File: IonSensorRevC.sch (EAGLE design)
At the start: 19 parts, among them U1 REF2033AIDDCT, U2 INA826AIDR, U3 INA826AIDR, U4 INA826AIDR, X1 SFV4R-1STE1LF

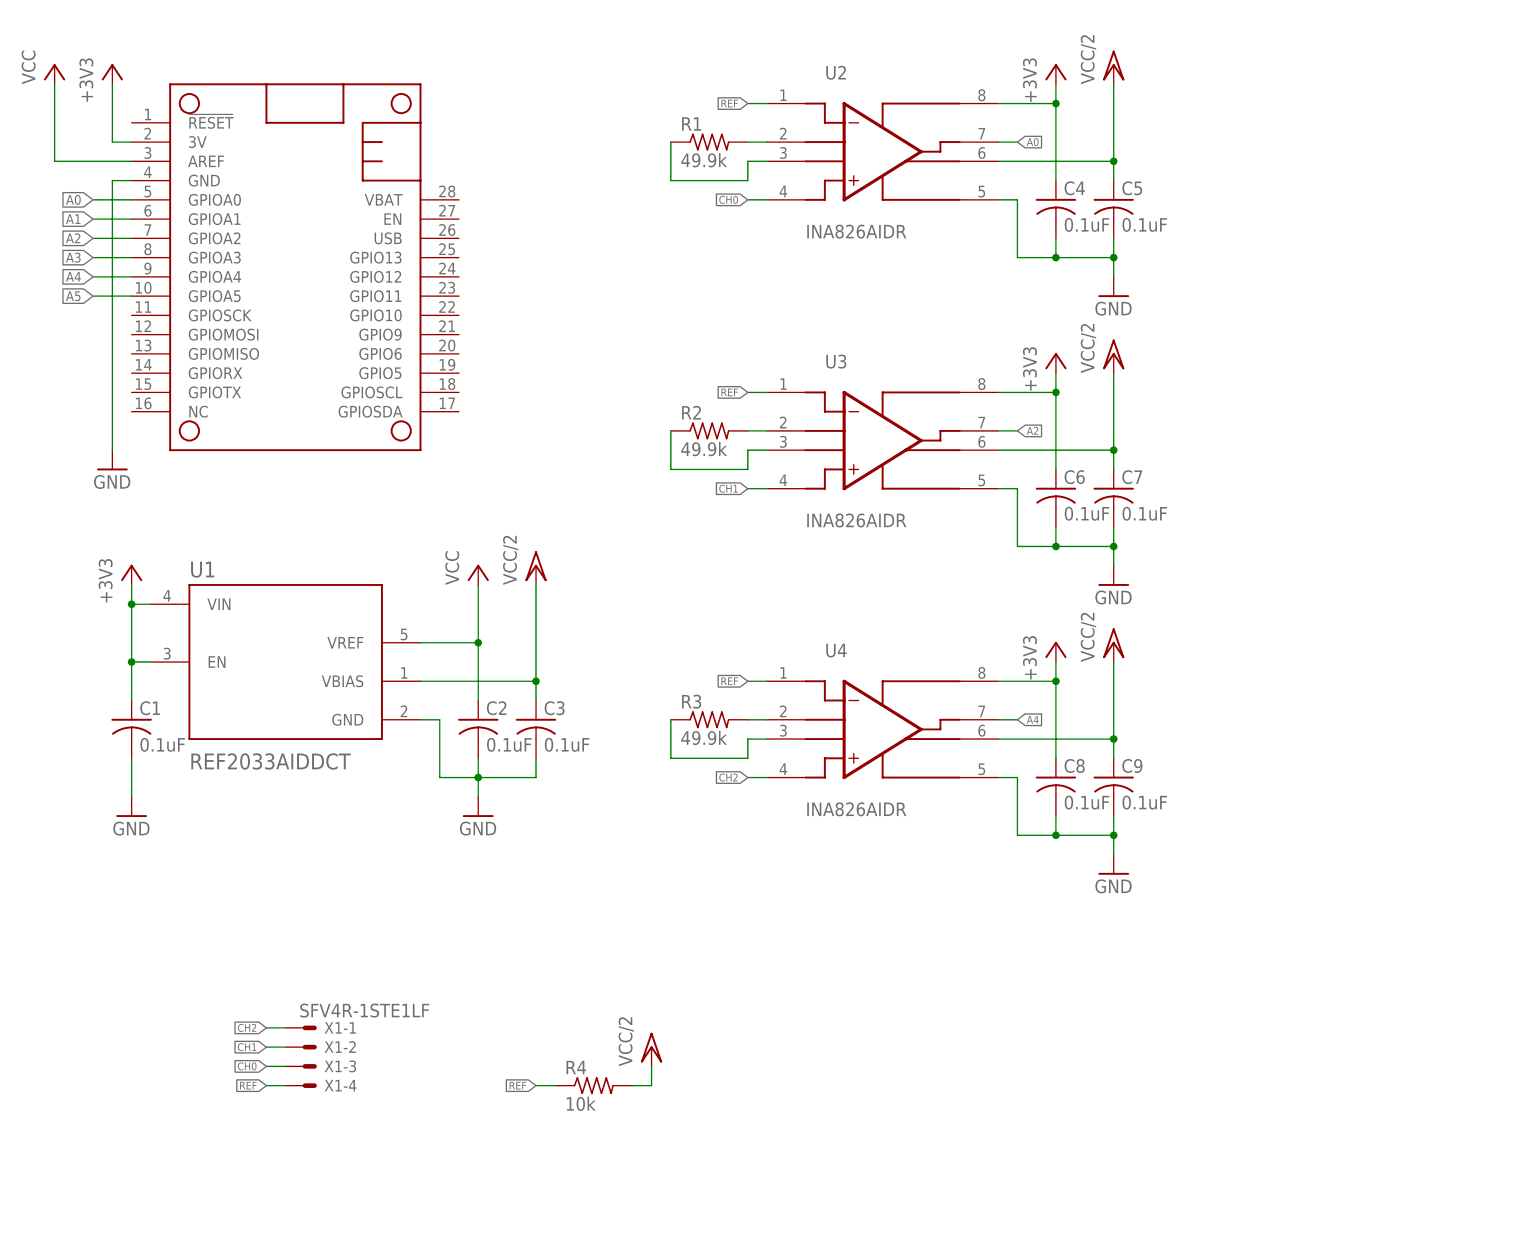
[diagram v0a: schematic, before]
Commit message: Update traces
Updated traces to minimize noise
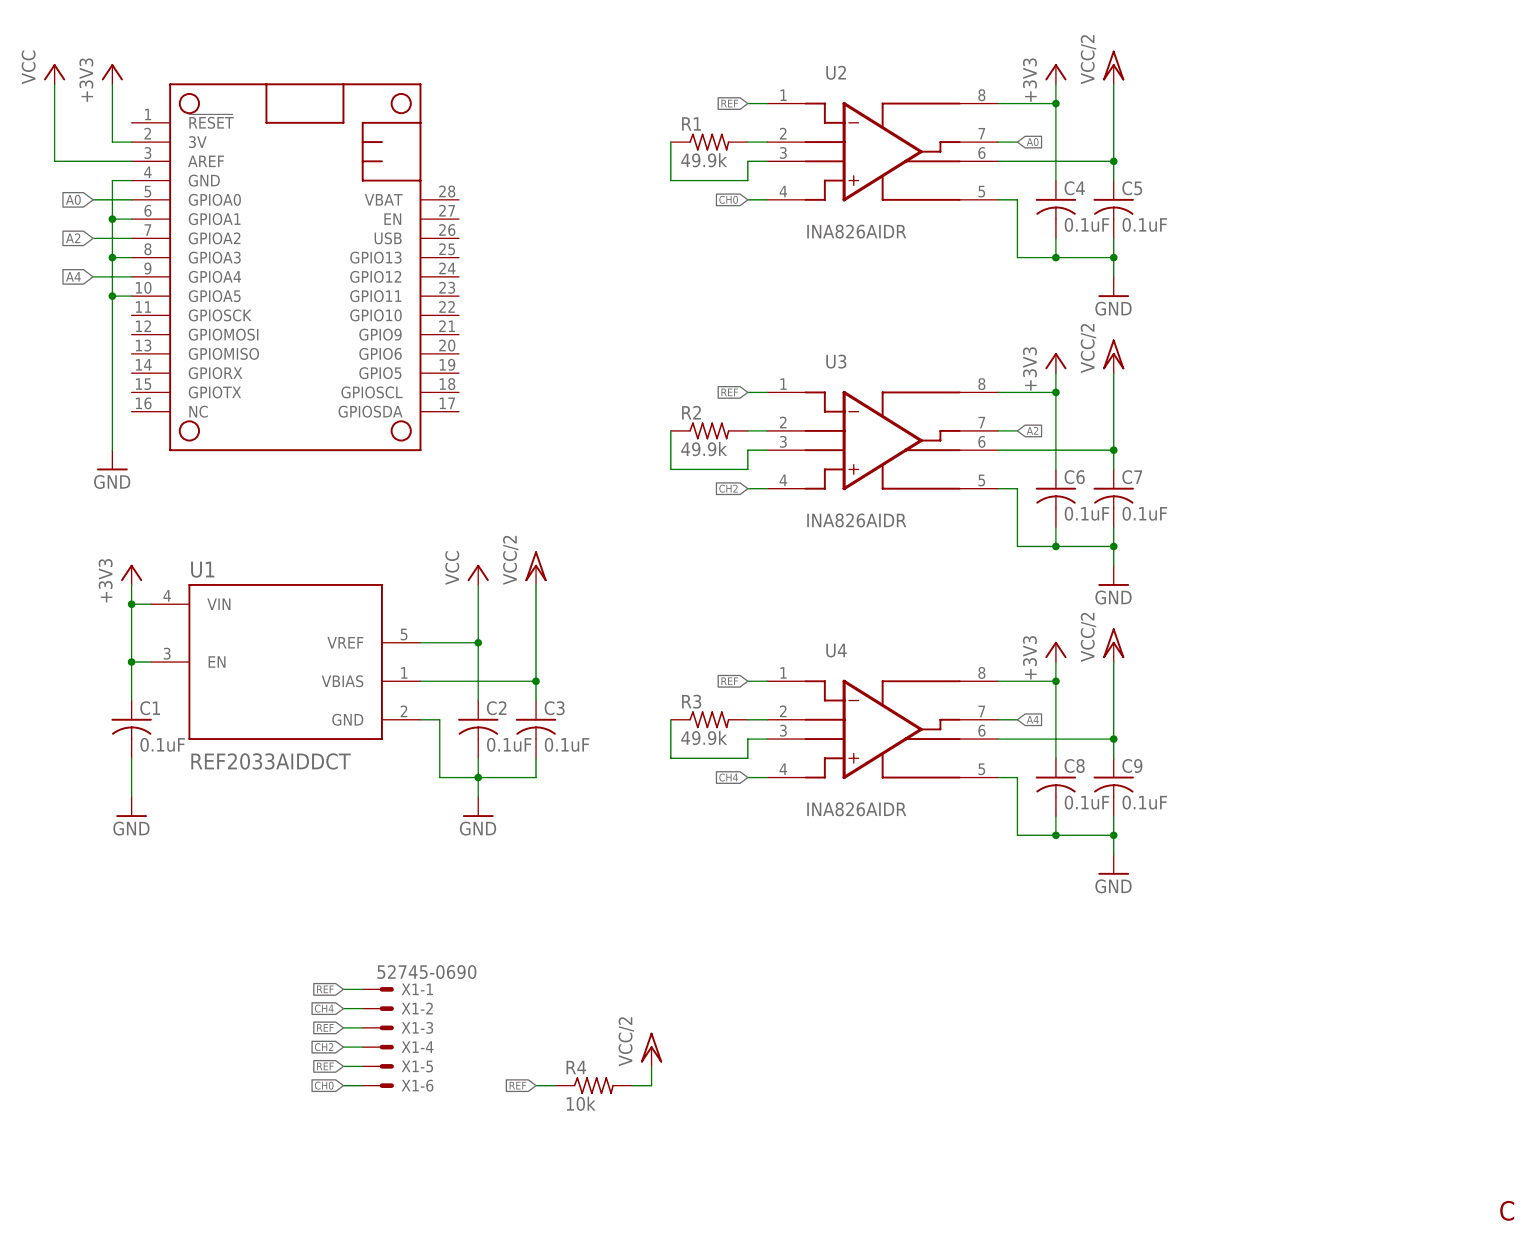
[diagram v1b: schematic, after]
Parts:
- X1: value SFV4R-1STE1LF -> 52745-0690; device adafruit:SFV4R-1STE1LF -> con-molex:52745-0690
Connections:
- removed net A1: MS1.GPIOA1
- removed net A3: MS1.GPIOA3
- removed net A5: MS1.GPIOA5
- removed net CH1: U3.+IN, X1-2.S
- new net CH4: U4.+IN, X1-2.S
- net CH0: now also X1-6.S; no longer X1-3.S
- net CH2: now also U3.+IN, X1-4.S; no longer U4.+IN, X1-1.S
- net GND: now also MS1.GPIOA1, MS1.GPIOA3, MS1.GPIOA5
- net REF: now also X1-1.S, X1-3.S, X1-5.S; no longer X1-4.S
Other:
- note added: "C"
- moved on the sheet: X1-1, X1-2, X1-3, X1-4
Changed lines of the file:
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@@
 <part name="C8" library="adafruit" library_urn="urn:adsk.eagle:library:420" deviceset="C-US" device="C0402" package3d_urn="urn:adsk.eagle:package:6240340/1" value="0.1uF"/>
 <part name="C9" library="adafruit" library_urn="urn:adsk.eagle:library:420" deviceset="C-US" device="C0402" package3d_urn="urn:adsk.eagle:package:6240340/1" value="0.1uF"/>
-<part name="X1" library="adafruit" library_urn="urn:adsk.eagle:library:420" deviceset="SFV4R-1STE1LF" device="" package3d_urn="urn:adsk.eagle:package:6240802/1"/>
 <part name="R4" library="adafruit" library_urn="urn:adsk.eagle:library:420" deviceset="R-US_" device="R0402" package3d_urn="urn:adsk.eagle:package:6240564/1" value="10k"/>
 <part name="P+7" library="supply1" library_urn="urn:adsk.eagle:library:371" deviceset="VCC/2" device=""/>
+<part name="X1" library="con-molex" library_urn="urn:adsk.eagle:library:165" deviceset="52745-0690" device="" package3d_urn="urn:adsk.eagle:package:8078608/1"/>
 </parts>
 <sheets>
 <sheet>
 <plain>
+<text x="238.76" y="7.62" size="2.54" layer="94">C</text>
 </plain>
 <instances>
@@
 <attribute name="VALUE" x="188.976" y="61.849" size="1.778" layer="96"/>
 </instance>
-<instance part="X1" gate="-1" x="81.28" y="33.02" smashed="yes">
-<attribute name="NAME" x="83.82" y="32.258" size="1.524" layer="95"/>
-<attribute name="VALUE" x="80.518" y="34.417" size="1.778" layer="96"/>
-</instance>
-<instance part="X1" gate="-2" x="81.28" y="30.48" smashed="yes">
-<attribute name="NAME" x="83.82" y="29.718" size="1.524" layer="95"/>
-</instance>
-<instance part="X1" gate="-3" x="81.28" y="27.94" smashed="yes">
-<attribute name="NAME" x="83.82" y="27.178" size="1.524" layer="95"/>
-</instance>
-<instance part="X1" gate="-4" x="81.28" y="25.4" smashed="yes">
-<attribute name="NAME" x="83.82" y="24.638" size="1.524" layer="95"/>
-</instance>
 <instance part="R4" gate="G$1" x="119.38" y="25.4" smashed="yes">
 <attribute name="NAME" x="115.57" y="26.8986" size="1.778" layer="95"/>
@@
 <instance part="P+7" gate="G$1" x="127" y="30.48" smashed="yes">
 <attribute name="VALUE" x="124.46" y="27.94" size="1.778" layer="96" rot="R90"/>
+</instance>
+<instance part="X1" gate="-1" x="91.44" y="38.1" smashed="yes">
+<attribute name="NAME" x="93.98" y="37.338" size="1.524" layer="95"/>
+<attribute name="VALUE" x="90.678" y="39.497" size="1.778" layer="96"/>
+</instance>
+<instance part="X1" gate="-2" x="91.44" y="35.56" smashed="yes">
+<attribute name="NAME" x="93.98" y="34.798" size="1.524" layer="95"/>
+</instance>
+<instance part="X1" gate="-3" x="91.44" y="33.02" smashed="yes">
+<attribute name="NAME" x="93.98" y="32.258" size="1.524" layer="95"/>
+</instance>
+<instance part="X1" gate="-4" x="91.44" y="30.48" smashed="yes">
+<attribute name="NAME" x="93.98" y="29.718" size="1.524" layer="95"/>
+</instance>
+<instance part="X1" gate="-5" x="91.44" y="27.94" smashed="yes">
+<attribute name="NAME" x="93.98" y="27.178" size="1.524" layer="95"/>
+</instance>
+<instance part="X1" gate="-6" x="91.44" y="25.4" smashed="yes">
+<attribute name="NAME" x="93.98" y="24.638" size="1.524" layer="95"/>
 </instance>
 </instances>
@@
 <wire x1="58.42" y1="144.78" x2="55.88" y2="144.78" width="0.1524" layer="91"/>
 <pinref part="GND1" gate="1" pin="GND"/>
-<wire x1="55.88" y1="144.78" x2="55.88" y2="109.22" width="0.1524" layer="91"/>
+<wire x1="55.88" y1="144.78" x2="55.88" y2="139.7" width="0.1524" layer="91"/>
+<pinref part="MS1" gate="G$1" pin="GPIOA1"/>
+<wire x1="55.88" y1="139.7" x2="55.88" y2="134.62" width="0.1524" layer="91"/>
+<wire x1="55.88" y1="134.62" x2="55.88" y2="129.54" width="0.1524" layer="91"/>
+<wire x1="55.88" y1="129.54" x2="55.88" y2="109.22" width="0.1524" layer="91"/>
+<wire x1="58.42" y1="139.7" x2="55.88" y2="139.7" width="0.1524" layer="91"/>
+<junction x="55.88" y="139.7"/>
+<pinref part="MS1" gate="G$1" pin="GPIOA3"/>
+<wire x1="58.42" y1="134.62" x2="55.88" y2="134.62" width="0.1524" layer="91"/>
+<junction x="55.88" y="134.62"/>
+<pinref part="MS1" gate="G$1" pin="GPIOA5"/>
+<wire x1="58.42" y1="129.54" x2="55.88" y2="129.54" width="0.1524" layer="91"/>
+<junction x="55.88" y="129.54"/>
 </segment>
 <segment>
@@
 </segment>
 </net>
-<net name="A1" class="0">
-<segment>
-<pinref part="MS1" gate="G$1" pin="GPIOA1"/>
-<wire x1="53.34" y1="139.7" x2="58.42" y2="139.7" width="0.1524" layer="91"/>
-<label x="53.34" y="139.7" size="1.27" layer="95" rot="R180" xref="yes"/>
-</segment>
-</net>
 <net name="A2" class="0">
 <segment>
@@
 </segment>
 </net>
-<net name="A3" class="0">
-<segment>
-<pinref part="MS1" gate="G$1" pin="GPIOA3"/>
-<wire x1="53.34" y1="134.62" x2="58.42" y2="134.62" width="0.1524" layer="91"/>
-<label x="53.34" y="134.62" size="1.27" layer="95" rot="R180" xref="yes"/>
-</segment>
-</net>
 <net name="A4" class="0">
 <segment>
@@
 <wire x1="175.26" y1="73.66" x2="172.72" y2="73.66" width="0.1524" layer="91"/>
 <label x="175.26" y="73.66" size="1.016" layer="95" xref="yes"/>
-</segment>
-</net>
-<net name="A5" class="0">
-<segment>
-<pinref part="MS1" gate="G$1" pin="GPIOA5"/>
-<wire x1="53.34" y1="129.54" x2="58.42" y2="129.54" width="0.1524" layer="91"/>
-<label x="53.34" y="129.54" size="1.27" layer="95" rot="R180" xref="yes"/>
 </segment>
 </net>
@@
 </segment>
 <segment>
-<pinref part="X1" gate="-4" pin="S"/>
-<wire x1="76.2" y1="25.4" x2="78.74" y2="25.4" width="0.1524" layer="91"/>
-<label x="76.2" y="25.4" size="1.016" layer="95" rot="R180" xref="yes"/>
-</segment>
-<segment>
 <pinref part="R4" gate="G$1" pin="1"/>
 <wire x1="111.76" y1="25.4" x2="114.3" y2="25.4" width="0.1524" layer="91"/>
 <label x="111.76" y="25.4" size="1.016" layer="95" rot="R180" xref="yes"/>
+</segment>
+<segment>
+<pinref part="X1" gate="-5" pin="S"/>
+<wire x1="86.36" y1="27.94" x2="88.9" y2="27.94" width="0.1524" layer="91"/>
+<label x="86.36" y="27.94" size="1.016" layer="95" rot="R180" xref="yes"/>
+</segment>
+<segment>
+<pinref part="X1" gate="-3" pin="S"/>
+<wire x1="86.36" y1="33.02" x2="88.9" y2="33.02" width="0.1524" layer="91"/>
+<label x="86.36" y="33.02" size="1.016" layer="95" rot="R180" xref="yes"/>
+</segment>
+<segment>
+<pinref part="X1" gate="-1" pin="S"/>
+<wire x1="86.36" y1="38.1" x2="88.9" y2="38.1" width="0.1524" layer="91"/>
+<label x="86.36" y="38.1" size="1.016" layer="95" rot="R180" xref="yes"/>
 </segment>
 </net>
@@
 </segment>
 <segment>
-<pinref part="X1" gate="-3" pin="S"/>
-<wire x1="76.2" y1="27.94" x2="78.74" y2="27.94" width="0.1524" layer="91"/>
-<label x="76.2" y="27.94" size="1.016" layer="95" rot="R180" xref="yes"/>
-</segment>
-</net>
-<net name="CH1" class="0">
+<pinref part="X1" gate="-6" pin="S"/>
+<wire x1="86.36" y1="25.4" x2="88.9" y2="25.4" width="0.1524" layer="91"/>
+<label x="86.36" y="25.4" size="1.016" layer="95" rot="R180" xref="yes"/>
+</segment>
+</net>
+<net name="CH2" class="0">
 <segment>
 <pinref part="U3" gate="G$1" pin="+IN"/>
@@
 </segment>
 <segment>
-<pinref part="X1" gate="-2" pin="S"/>
-<wire x1="76.2" y1="30.48" x2="78.74" y2="30.48" width="0.1524" layer="91"/>
-<label x="76.2" y="30.48" size="1.016" layer="95" rot="R180" xref="yes"/>
-</segment>
-</net>
-<net name="CH2" class="0">
+<pinref part="X1" gate="-4" pin="S"/>
+<wire x1="86.36" y1="30.48" x2="88.9" y2="30.48" width="0.1524" layer="91"/>
+<label x="86.36" y="30.48" size="1.016" layer="95" rot="R180" xref="yes"/>
+</segment>
+</net>
+<net name="CH4" class="0">
 <segment>
 <pinref part="U4" gate="G$1" pin="+IN"/>
@@
 </segment>
 <segment>
-<pinref part="X1" gate="-1" pin="S"/>
-<wire x1="76.2" y1="33.02" x2="78.74" y2="33.02" width="0.1524" layer="91"/>
-<label x="76.2" y="33.02" size="1.016" layer="95" rot="R180" xref="yes"/>
-</segment>
-</net>
+<pinref part="X1" gate="-2" pin="S"/>
+<wire x1="86.36" y1="35.56" x2="88.9" y2="35.56" width="0.1524" layer="91"/>
+<label x="86.36" y="35.56" size="1.016" layer="95" rot="R180" xref="yes"/>
+</segment>
+</net>
